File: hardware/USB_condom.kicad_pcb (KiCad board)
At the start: 2 copper layers, 4 parts, among them J1 USB_A, J2 USB_A, U1 TPS2514A

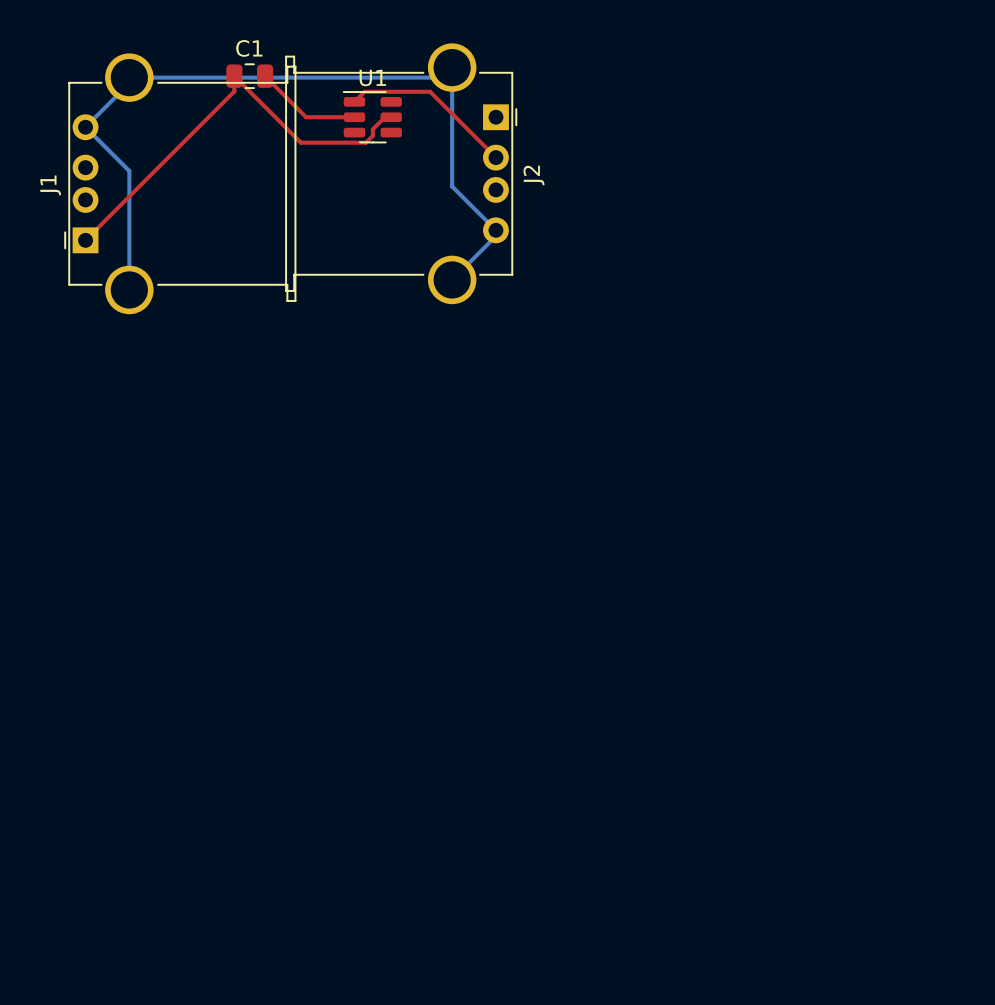
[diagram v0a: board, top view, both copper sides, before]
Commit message: update project add schematic and first layout
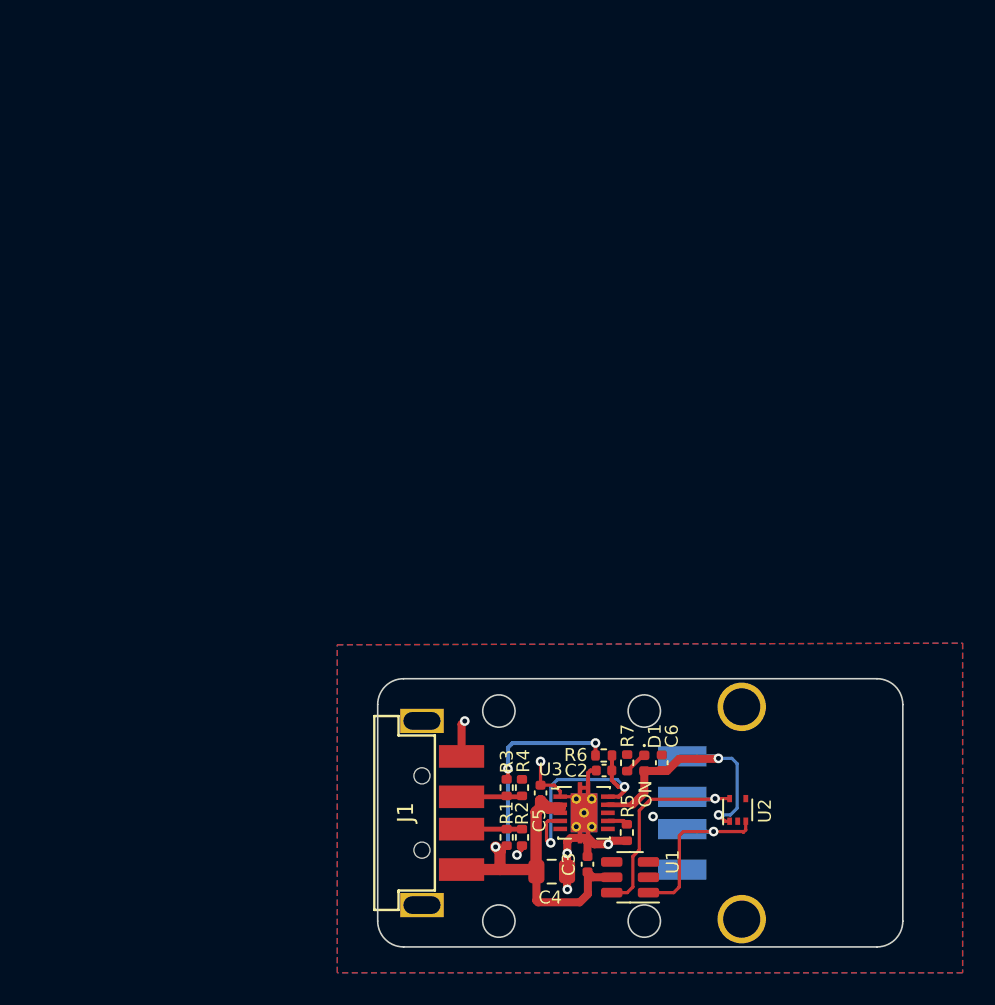
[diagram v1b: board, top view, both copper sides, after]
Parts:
- removed C1: 0.1uF, Capacitor_SMD:C_0805_2012Metric
- added C2: 0.22uF, Capacitor_SMD:C_0402_1005Metric, F.Cu at (141.3, 91.2)
- added C3: 0.1uF, Capacitor_SMD:C_0402_1005Metric, F.Cu at (140.3, 97.0)
- added C4: 10uF, Capacitor_SMD:C_0805_2012Metric, F.Cu at (138.1, 97.5)
- added C5: 0.1uF, Capacitor_SMD:C_0402_1005Metric, F.Cu at (137.4, 92.6)
- added C6: 0.1uF, Capacitor_SMD:C_0402_1005Metric, F.Cu at (144.9, 90.8)
- added D1: ON, LED_SMD:LED_0402_1005Metric, F.Cu at (143.8, 90.8)
- added R1: 43.2K, Resistor_SMD:R_0402_1005Metric, F.Cu at (135.3, 95.4)
- added R2: 49.9K, Resistor_SMD:R_0402_1005Metric, F.Cu at (136.2, 95.4)
- added R3: 75K, Resistor_SMD:R_0402_1005Metric, F.Cu at (135.3, 92.3)
- added R4: 49.9K, Resistor_SMD:R_0402_1005Metric, F.Cu at (136.2, 92.3)
- added R5: 20K, Resistor_SMD:R_0402_1005Metric, F.Cu at (142.7, 95.1)
- added R6: 100K, Resistor_SMD:R_0402_1005Metric, F.Cu at (141.3, 90.3)
- added R7: 1K, Resistor_SMD:R_0402_1005Metric, F.Cu at (142.7, 90.8)
- added U2: TPD2E001, Package_TO_SOT_SMD:SOT-553, F.Cu at (149.6, 93.7)
- added U3: TPS2561, Package_SON:VSON-10-1EP_3x3mm_P0.5mm_EP1.65x2.4mm_ThermalVias, F.Cu at (140.1, 93.8)
- J1: footprint Connector_USB:USB_A_Stewart_SS-52100-001_Horizontal -> usbCondom:C46394
- J2: footprint Connector_USB:USB_A_Stewart_SS-52100-001_Horizontal -> Connector_USB:USB_A_TE_292303-7_Horizontal; moved to B.Cu
- moved U1 49.7 mm to (142.9, 97.8), turned to 180 degrees
- moved J2 46.6 mm to (152.5, 93.9)
- moved J1 42.4 mm to (132.5, 93.9)
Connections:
- J1 pad 2: unconnected-(J1-Pad2) -> /DCP-
- J1 pad 3: unconnected-(J1-Pad3) -> /DCP+
- J2 pad 1: +5V -> VBUS
- J2 pad 2: /DP1 -> /D-
- J2 pad 3: /DM1 -> /D+
- U1 pad 1: /DP1 -> /D+
- U1 pad 6: /DM1 -> /D-
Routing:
- net GND: track 57.6 -> 17.5 mm, vias 0 -> 7
- net VBUS: track 0.00 -> 17.3 mm, vias 0 -> 2
- net /FAULT: track 0.00 -> 14.8 mm, vias 0 -> 2
- net /D-: track 0.00 -> 14.3 mm, vias 0 -> 1
- net /D+: track 0.00 -> 12.0 mm, vias 0 -> 1
- net /DP1: track 10.7 -> 0.00 mm
- net +5V: track 26.3 -> 34.9 mm, vias 0 -> 3
- net /DCP-: track 0.00 -> 8.41 mm
- net /DCP+: track 0.00 -> 3.76 mm
- net Net-(D1-K): track 0.00 -> 1.46 mm
- net Net-(U3-ILM): track 0.00 -> 1.26 mm
- added copper zone on B.Cu, net GND
- added copper zone on F.Cu, net GND
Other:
- board outline added: 32.5 x 16.6 mm

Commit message: update labels
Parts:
- added G***: LOGO, Symbol_EC:electronic_cats_logo_4x3, F.Cu at (155.9, 93.3)
- added G***: LOGO, Symbol_EC:electronic_cats_logo_8x6, B.Cu at (139.4, 92.0)
- added kibuzzard-644073E0: G***, kibuzzard-644073E0, F.Cu at (155.7, 97.1)
- added kibuzzard-644073E0: G***, kibuzzard-644073E0, B.Cu at (139.4, 96.4)
- added kibuzzard-64407430: G***, kibuzzard-64407430, F.Cu at (155.6, 98.9)
- added kibuzzard-64407430: G***, kibuzzard-64407430, B.Cu at (139.5, 98.3)
- added kibuzzard-644074B7: G***, kibuzzard-644074B7, B.Cu at (139.8, 100.6)
- added kibuzzard-644074E2: G***, kibuzzard-644074E2, B.Cu at (138.9, 87.5)

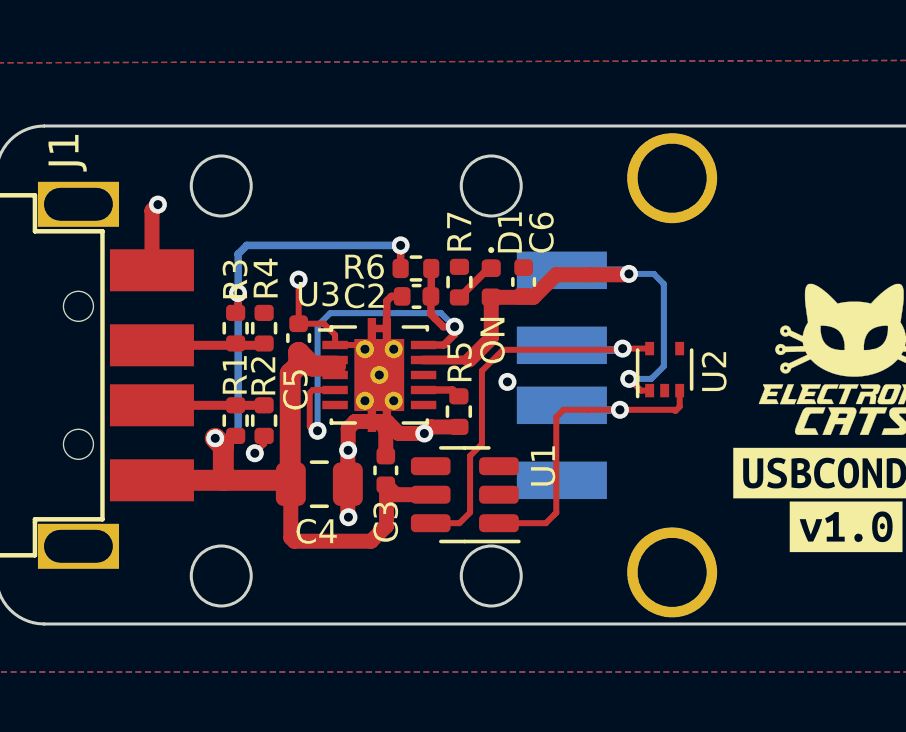
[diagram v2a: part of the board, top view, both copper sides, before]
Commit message: add capacitor, add LCSC numbers
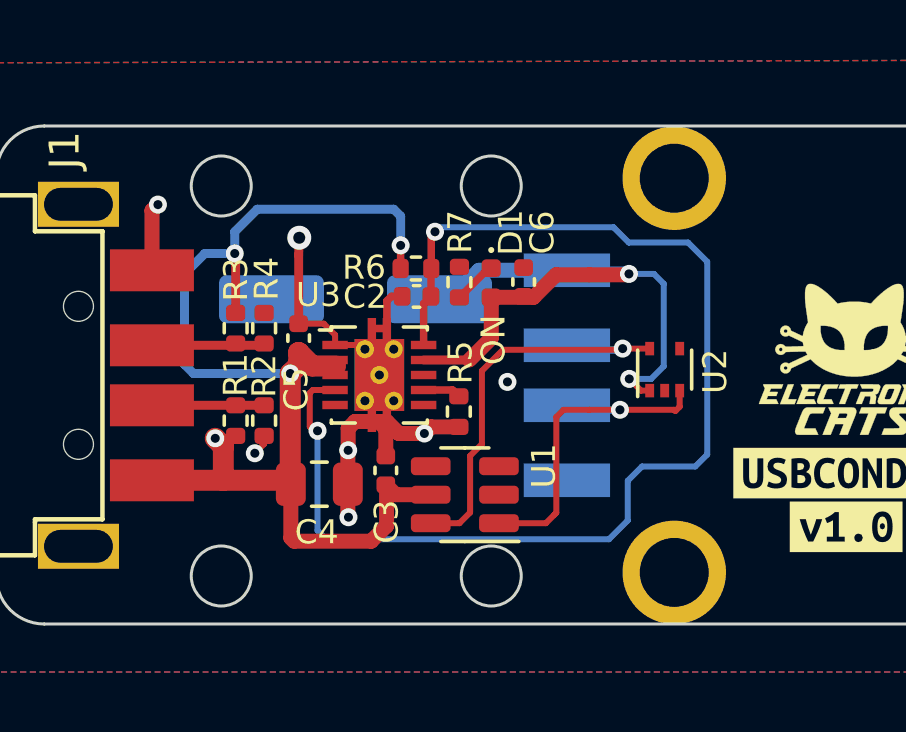
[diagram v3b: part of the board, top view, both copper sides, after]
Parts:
- removed kibuzzard-644074B7: G***, kibuzzard-644074B7
- removed kibuzzard-644074E2: G***, kibuzzard-644074E2
- added C1: 150uF, Capacitor_SMD:CP_Elec_6.3x5.4, B.Cu at (139.3, 91.3)
- J2: footprint Connector_USB:USB_A_TE_292303-7_Horizontal -> usbCondom:875832010BLF
- moved kibuzzard-644073E0 8.07 mm to (131.8, 93.6), turned to -90 degrees
- moved kibuzzard-64407430 7.61 mm to (133.6, 93.5), turned to -90 degrees
- moved G*** 6.75 mm to (139.2, 98.7), turned to 0 degrees
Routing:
- net /FAULT: track 14.8 -> 40.8 mm
- net +5V: track 34.9 -> 40.1 mm, vias 3 -> 4
- net VBUS: track 17.3 -> 21.8 mm
- net GND: track 17.5 -> 18.9 mm
